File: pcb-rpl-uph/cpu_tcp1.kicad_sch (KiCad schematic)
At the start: 1 part, among them U5 RPL_UPH_FCBGA1744

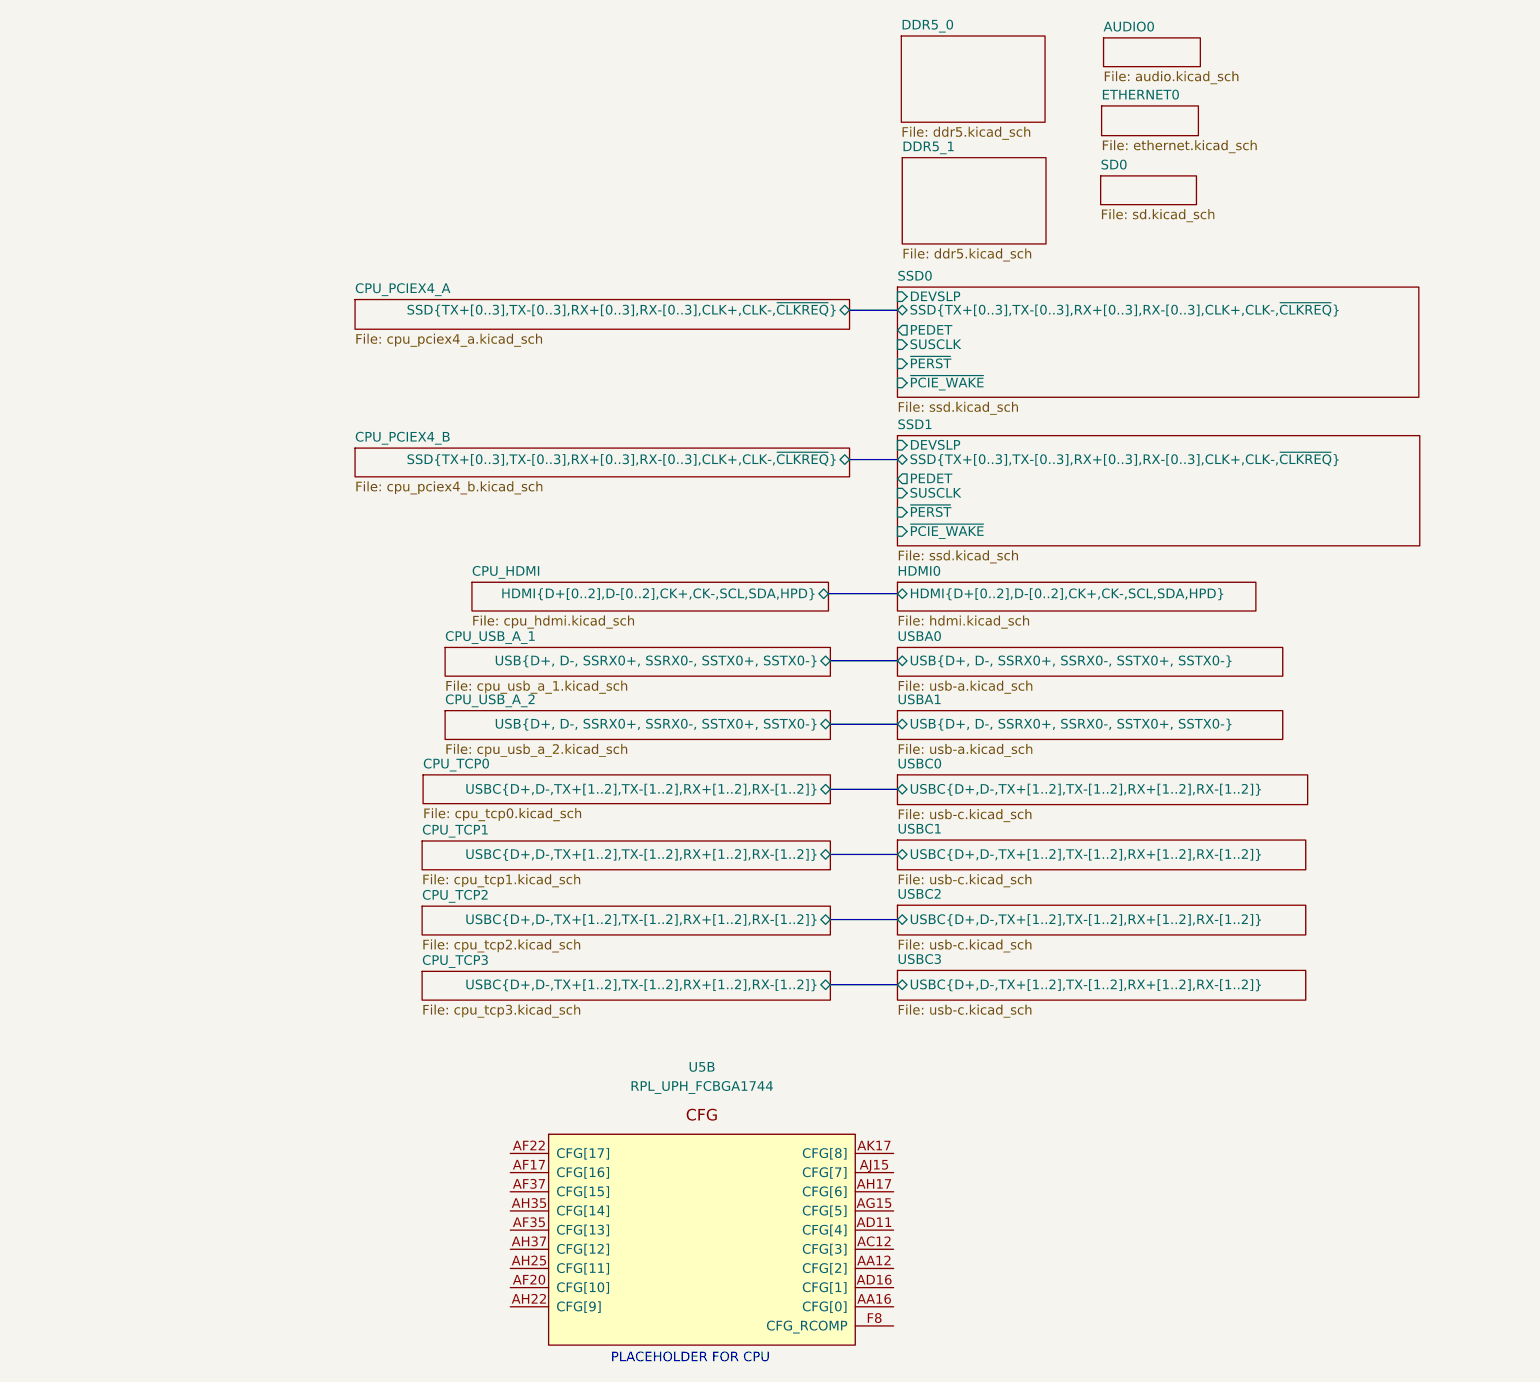
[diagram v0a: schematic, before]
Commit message: Connect USB-A and USB-C data
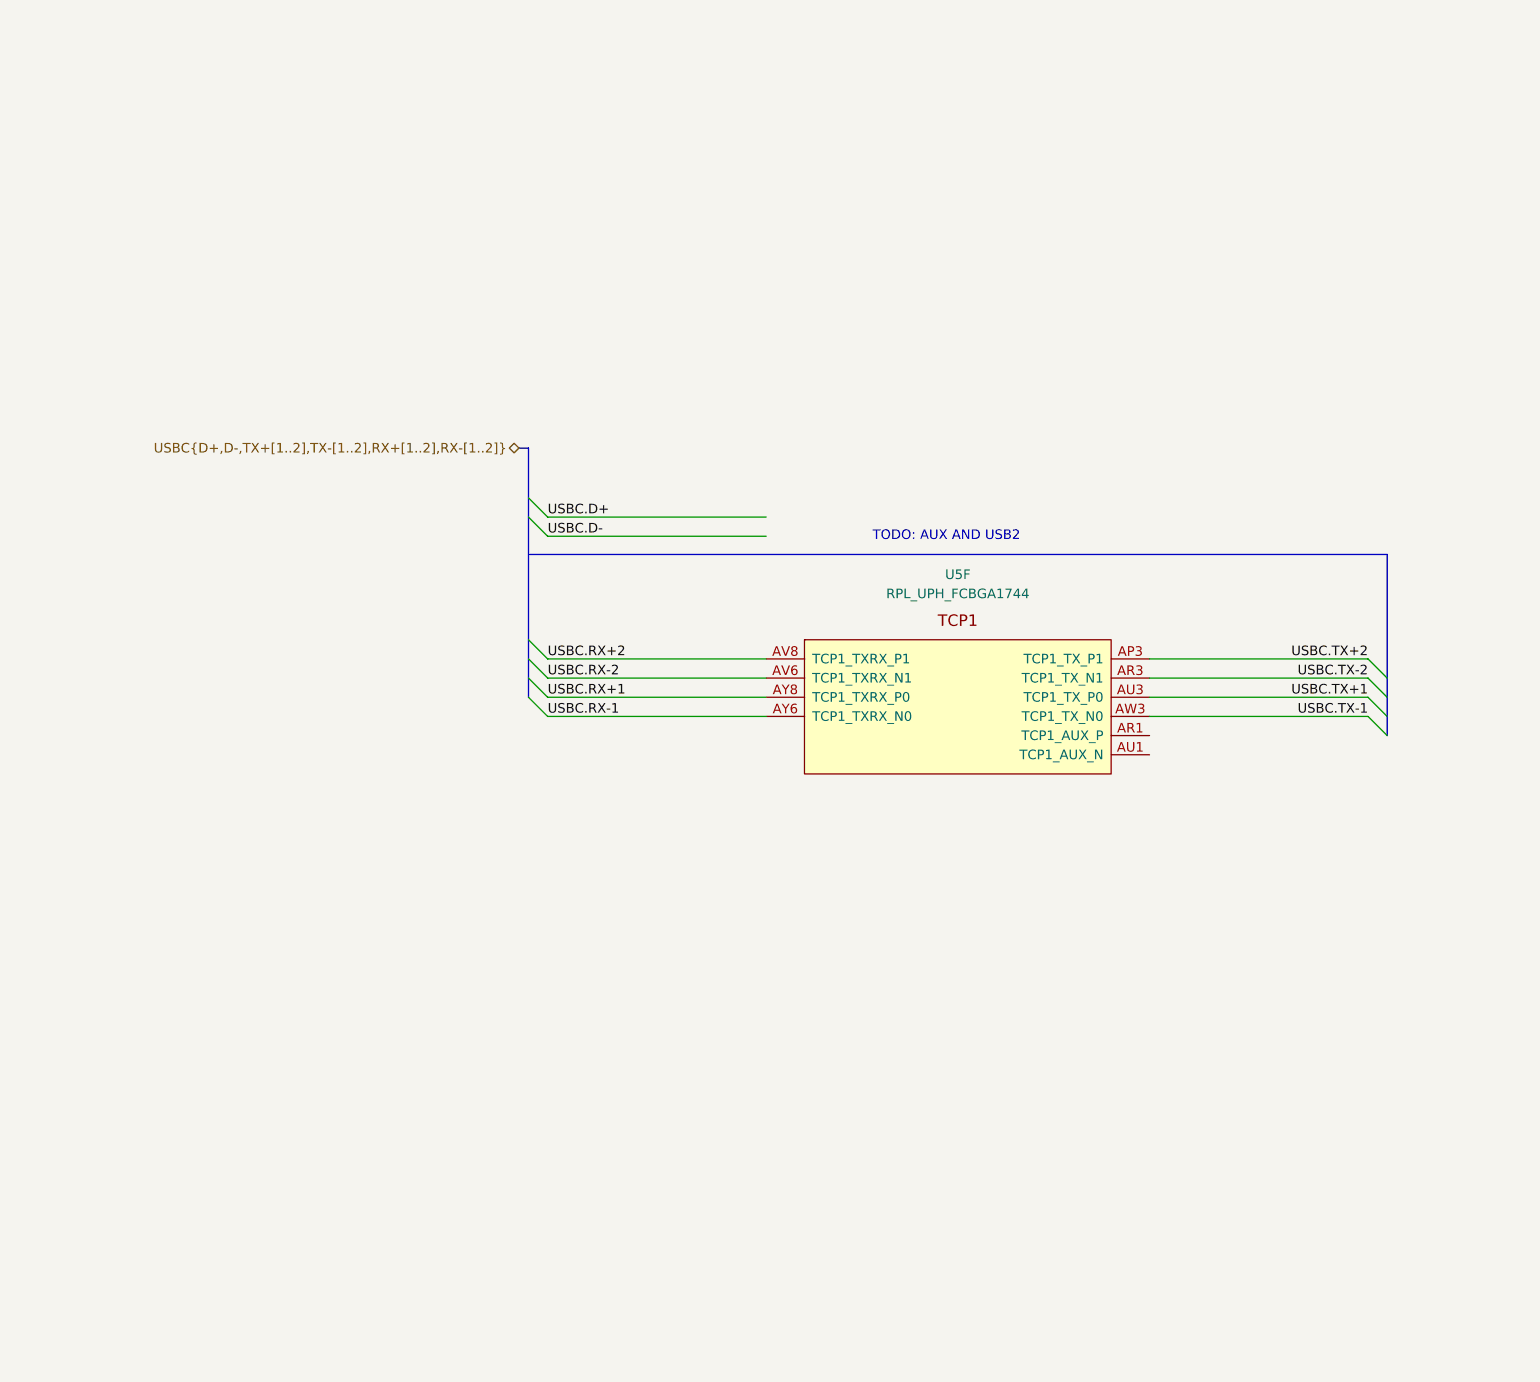
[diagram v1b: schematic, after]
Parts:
- removed U5: RPL_UPH_FCBGA1744, local:RPL_UPH_FCBGA1744, symbol local:RPL_UPH_FCBGA1744
- added U5: RPL_UPH_FCBGA1744, symbol local:RPL_UPH_FCBGA1744
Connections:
- new net USBC.RX+1: U5.AY8 (TCP1_TXRX_P0)
- new net USBC.RX+2: U5.AV8 (TCP1_TXRX_P1)
- new net USBC.RX-1: U5.AY6 (TCP1_TXRX_N0)
- new net USBC.RX-2: U5.AV6 (TCP1_TXRX_N1)
- new net USBC.TX+1: U5.AU3 (TCP1_TX_P0)
- new net USBC.TX+2: U5.AP3 (TCP1_TX_P1)
- new net USBC.TX-1: U5.AW3 (TCP1_TX_N0)
- new net USBC.TX-2: U5.AR3 (TCP1_TX_N1)
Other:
- removed sheet AUDIO0
- removed sheet CPU_HDMI
- removed sheet CPU_PCIEX4_A
- removed sheet CPU_PCIEX4_B
- removed sheet CPU_TCP0
- removed sheet CPU_TCP1
- removed sheet CPU_TCP2
- removed sheet CPU_TCP3
- removed sheet CPU_USB_A_1
- removed sheet CPU_USB_A_2
- removed sheet DDR5_0
- removed sheet DDR5_1
- removed sheet ETHERNET0
- removed sheet HDMI0
- removed sheet SD0
- removed sheet SSD0
- removed sheet SSD1
- removed sheet USBA0
- removed sheet USBA1
- removed sheet USBC0
- removed sheet USBC1
- removed sheet USBC2
- removed sheet USBC3
- note added: "TODO: AUX AND USB2"
- note removed: "PLACEHOLDER FOR CPU"

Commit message: add display connector
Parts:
- U5: footprint (none) -> local:RPL_UPH_FCBGA1744
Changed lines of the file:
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@@
       (effects (font (size 1.27 1.27)))
     )
-    (property "Footprint" "" (at 150.241 92.456 0)
+    (property "Footprint" "local:RPL_UPH_FCBGA1744" (at 150.241 92.456 0)
       (effects (font (size 1.27 1.27)) hide)
     )
